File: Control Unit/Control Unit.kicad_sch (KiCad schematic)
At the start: 17 parts, among them J1 PWR_IN, J2 LM2596S, J3 ST7789, J4 DHT20, J5 RTC, J6 RPM_IN, J7 Page flip, SW1 SW_DPST_x2, U1 ESP32-DEVKIT-V1, U2 PC817

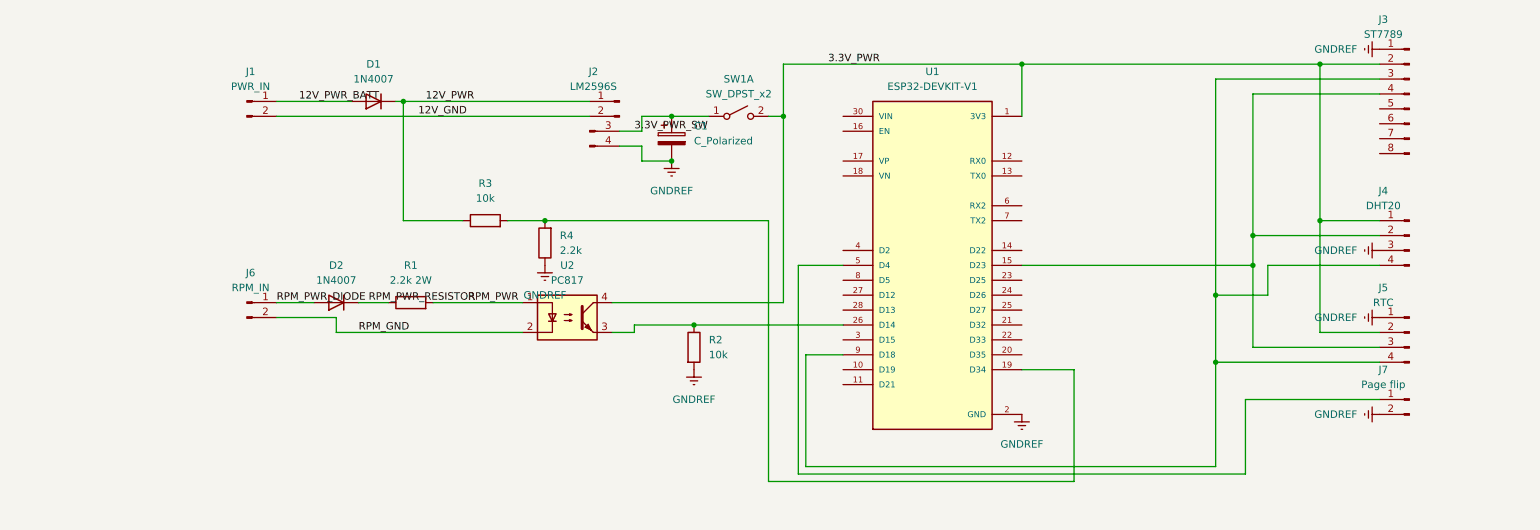
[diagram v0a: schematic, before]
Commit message: rev 1.1: added relay to use power directly from battery
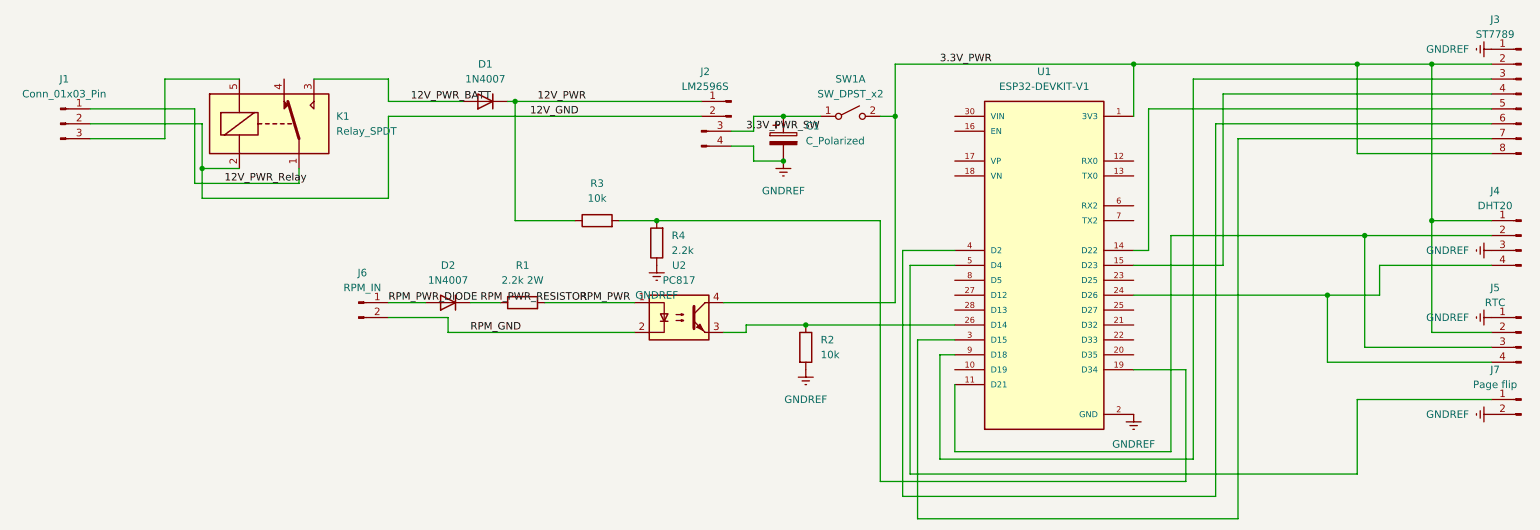
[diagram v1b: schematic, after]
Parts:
- removed J1: PWR_IN, Connector_Wire:SolderWire-1.5sqmm_1x02_P7.8mm_D1.7mm_OD3.9mm_Relief, symbol Connector:Conn_01x02_Pin
- added J1: Conn_01x03_Pin, Connector_Wire:SolderWire-1.5sqmm_1x03_P6mm_D1.7mm_OD3mm, symbol Connector:Conn_01x03_Pin
- added K1: Relay_SPDT, Relay_THT:Relay_SPDT_SANYOU_SRD_Series_Form_C, symbol Relay:Relay_SPDT
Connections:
- net 12V_GND: now also J1.2 (GND), K1.2
- net 12V_PWR_BATT: now also K1.3
- net 3.3V_PWR: now also J3.8 (Pin_8)
- net at U1.11 (D21): now also J4.2 (SDA), J5.3 (SDA)
- net at U1.14 (D22): now also J3.5 (RES)
- net at J3.4 (SDA), U1.15 (D23): no longer J4.2 (SDA), J5.3 (SDA)
- net at U1.24 (D26): now also J4.4 (SCL), J5.4 (SCL)
- net at U1.3 (D15): now also J3.7 (CS)
- net at U1.4 (D2): now also J3.6 (DC)
- net at J3.3 (SCL), U1.9 (D18): no longer J4.4 (SCL), J5.4 (SCL)
- new net: J1.3 (12V_SWITCH), K1.5
- new net 12V_PWR_Relay: J1.1 (12V_PWR), K1.1
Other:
- moved on the sheet: C1, D1, D2, J2, J3, J4, J5, J6, J7, R1, R2, R3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
